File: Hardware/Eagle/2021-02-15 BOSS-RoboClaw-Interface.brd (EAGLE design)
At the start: 41.4 x 48.3 mm, 10 parts, among them IC1 ISO7221AQDRQ1, J1 MOLEX 22112024, J2 MOLEX 22122034, J3 Amphenol 75869-130LF, J5 SAMTEC ESQ-110-33-T-D, J6 SAMTEC-ESQ-105-33-T-S, X1 Amphenol L77SDAH15SOL2RM8C309

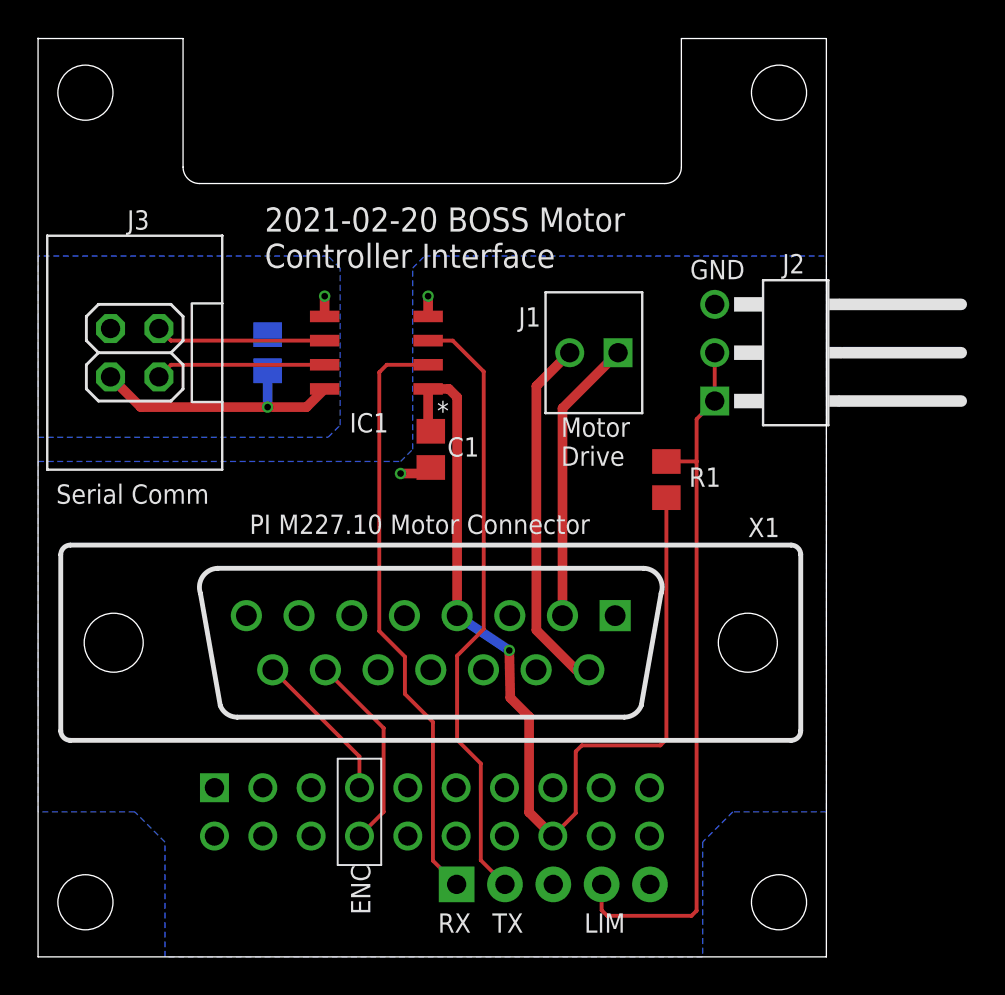
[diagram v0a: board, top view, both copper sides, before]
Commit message: Added pullup to limit switch line
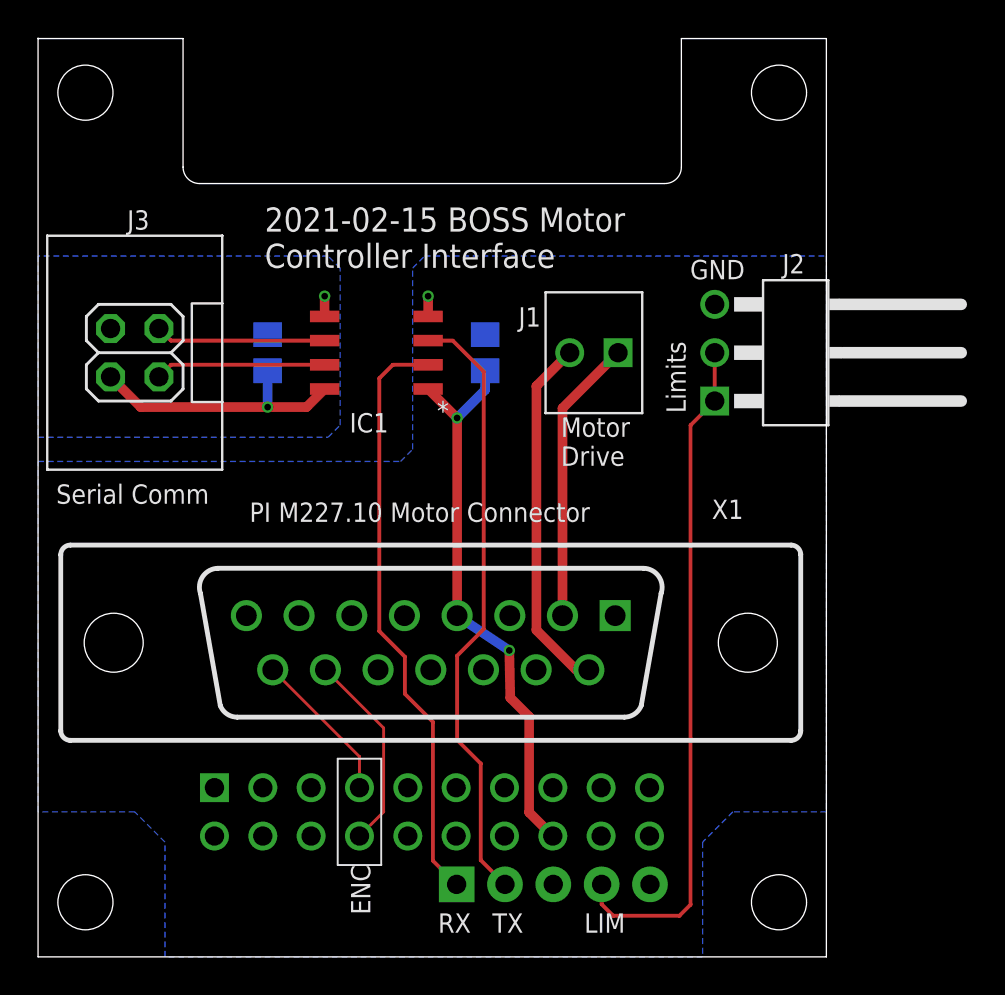
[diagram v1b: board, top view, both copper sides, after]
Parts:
- removed R1: 10K, AUmlib:R0805
- moved C1 5.83 mm to (23.5, 31.8), flipped to the bottom, turned to 90 degrees
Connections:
- removed net ROBO-RX: IC1.2, J6.1
- removed net ROBO0TX: IC1.3, J6.2
- new net RXMCU: IC1.6, J3.3
- new net TXMCU: IC1.7, J3.1
- net LIMIT: no longer R1.1
- net RX: now also IC1.2, J6.1; no longer IC1.7, J3.1
- net TX: now also IC1.3, J6.2; no longer IC1.6, J3.3
- net VCC1: no longer R1.2
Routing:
- net ROBO0TX: track 32.2 -> 0.00 mm
- net ROBO-RX: track 31.3 -> 0.00 mm
- net TX: track 8.98 -> 32.2 mm
- net VCC1: track 52.1 -> 29.6 mm, vias 1 -> 2
- net RX: track 8.98 -> 31.1 mm
- net RXMCU: track 0.00 -> 8.98 mm
- net TXMCU: track 0.00 -> 8.98 mm
- net LIMIT: track 37.9 -> 35.7 mm
- net GND: track 2.79 -> 1.07 mm, vias 2 -> 1
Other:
- board text added: "2021-02-15 BOSS Motor Controller Interface"
- board text added: "Limits"
- board text removed: "+5V"
- board text removed: "2021-02-20 BOSS Motor Controller Interface"
- board text removed: "GND -ISO"
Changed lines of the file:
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@@
 <wire x1="8.4836" y1="40.64" x2="32.9438" y2="40.64" width="0" layer="20"/>
 <wire x1="33.8074" y1="48.26" x2="41.4274" y2="48.26" width="0" layer="20"/>
-<text x="11.9126" y="36.2077" size="1.27" layer="21" font="vector">2021-02-20 BOSS Motor
+<text x="11.9126" y="36.2077" size="1.27" layer="21" font="vector">2021-02-15 BOSS Motor
 Controller Interface</text>
+<text x="34.036" y="28.575" size="1.016" layer="21" font="vector" rot="R90">Limits</text>
 <text x="34.2646" y="35.6108" size="1.016" layer="21" font="vector">GND</text>
 <text x="27.4828" y="25.8064" size="1.016" layer="21" font="vector">Motor
@@
 <wire x1="15.748" y1="4.826" x2="18.034" y2="4.826" width="0.1016" layer="21"/>
 <text x="0.9525" y="23.8125" size="1.016" layer="21" font="vector">Serial Comm</text>
-<text x="11.1125" y="22.225" size="1.016" layer="21" font="vector">PI M227.10 Motor Connector</text>
-<text x="9.2075" y="32.385" size="1.016" layer="22" rot="MR0">TX</text>
-<text x="9.2075" y="29.845" size="1.016" layer="22" rot="MR0">RX</text>
-<text x="4.7625" y="28.2575" size="1.016" layer="22" rot="MR0">+5V</text>
-<text x="5.08" y="34.29" size="1.016" layer="22" rot="MR0">GND
--ISO</text>
+<text x="11.1125" y="22.86" size="1.016" layer="21" font="vector">PI M227.10 Motor Connector</text>
 </plain>
 <attributes>
@@
 <attribute name="MF" value="" x="53.6575" y="10.16" size="1.778" layer="27" display="off"/>
 <attribute name="MPN" value="" x="53.6575" y="10.16" size="1.778" layer="27" display="off"/>
-<attribute name="NAME" x="37.3126" y="22.0599" size="1.016" layer="25"/>
+<attribute name="NAME" x="35.4076" y="23.0124" size="1.016" layer="25"/>
 <attribute name="OC_FARNELL" value="unknown" x="53.6575" y="10.16" size="1.778" layer="27" display="off"/>
 <attribute name="OC_NEWARK" value="unknown" x="53.6575" y="10.16" size="1.778" layer="27" display="off"/>
 </element>
-<element name="C1" library="AUmlib" library_urn="urn:adsk.eagle:library:9166017" package="C0805" package3d_urn="urn:adsk.eagle:package:4021265/3" value="0.1uF" x="20.6375" y="26.67" smashed="yes" rot="R270">
-<attribute name="NAME" x="23.1775" y="27.305" size="1.016" layer="25" font="vector" rot="R180"/>
-<attribute name="SPICEPREFIX" value="C" x="20.6375" y="26.67" size="1.778" layer="27" rot="R270" display="off"/>
+<element name="C1" library="AUmlib" library_urn="urn:adsk.eagle:library:9166017" package="C0805" package3d_urn="urn:adsk.eagle:package:4021265/3" value="0.1uF" x="23.495" y="31.75" smashed="yes" rot="MR90">
+<attribute name="NAME" x="24.13" y="33.9725" size="1.016" layer="26" font="vector" rot="MR0"/>
+<attribute name="SPICEPREFIX" value="C" x="23.495" y="31.75" size="1.778" layer="28" rot="MR90" display="off"/>
 </element>
 <element name="C2" library="AUmlib" library_urn="urn:adsk.eagle:library:9166017" package="C0805" package3d_urn="urn:adsk.eagle:package:4021265/3" value="0.1uF" x="12.065" y="31.75" smashed="yes" rot="MR90">
@@
 <element name="J5" library="AUmlib" library_urn="urn:adsk.eagle:library:9166017" package="2X10-ESQ-110-33-T-D" package3d_urn="urn:adsk.eagle:package:24929474/2" value="SAMTEC ESQ-110-33-T-D" x="20.701" y="7.62" smashed="yes" rot="MR180">
 <attribute name="NAME" x="5.7785" y="8.255" size="1.016" layer="26" rot="MR180"/>
-</element>
-<element name="R1" library="AUmlib" library_urn="urn:adsk.eagle:library:9166017" package="R0805" package3d_urn="urn:adsk.eagle:package:4021199/4" value="10K" x="33.02" y="25.0825" smashed="yes" rot="R270">
-<attribute name="NAME" x="35.8775" y="25.7175" size="1.016" layer="25" font="vector" rot="R180"/>
-<attribute name="SPICEPREFIX" value="R" x="33.02" y="25.0825" size="1.778" layer="27" rot="R270" display="off"/>
 </element>
 </elements>
@@
 <contactref element="X1" pad="6"/>
 <contactref element="J5" pad="15"/>
-<wire x1="20.6375" y1="25.72" x2="20.3175" y2="25.4" width="0.508" layer="1"/>
-<wire x1="20.3175" y1="25.4" x2="19.05" y2="25.4" width="0.508" layer="1"/>
-<via x="19.05" y="25.4" extent="1-16" drill="0.35"/>
-</signal>
-<signal name="ROBO-RX">
+</signal>
+<signal name="RX">
 <contactref element="IC1" pad="2"/>
 <wire x1="20.7518" y1="12.3444" x2="19.2786" y2="13.8176" width="0.2032" layer="1"/>
-<wire x1="18.3261" y1="31.115" x2="20.4978" y2="31.115" width="0.2032" layer="1"/>
+<wire x1="18.6436" y1="31.115" x2="20.4978" y2="31.115" width="0.2032" layer="1"/>
 <wire x1="20.7518" y1="5.0546" x2="20.7518" y2="12.3444" width="0.2032" layer="1"/>
 <wire x1="19.2786" y1="13.8176" x2="19.2786" y2="15.7734" width="0.2032" layer="1"/>
 <wire x1="19.2786" y1="15.7734" x2="17.9324" y2="17.1196" width="0.2032" layer="1"/>
-<wire x1="17.9324" y1="17.1196" x2="17.9324" y2="30.7213" width="0.2032" layer="1"/>
-<wire x1="17.9324" y1="30.7213" x2="18.3261" y2="31.115" width="0.2032" layer="1"/>
+<wire x1="17.9324" y1="17.1196" x2="17.9324" y2="30.4038" width="0.2032" layer="1"/>
+<wire x1="17.9324" y1="30.4038" x2="18.6436" y2="31.115" width="0.2032" layer="1"/>
 <contactref element="J6" pad="1"/>
 <wire x1="21.9964" y1="3.81" x2="20.7518" y2="5.0546" width="0.2032" layer="1"/>
 </signal>
-<signal name="ROBO0TX">
+<signal name="TX">
 <contactref element="IC1" pad="3"/>
 <wire x1="20.4978" y1="32.385" x2="21.7932" y2="32.385" width="0.2032" layer="1"/>
@@
 <contactref element="J2" pad="2"/>
 <wire x1="35.56" y1="31.75" x2="35.56" y2="29.21" width="0.2032" layer="1"/>
-<wire x1="35.56" y1="29.21" x2="34.6075" y2="28.257496875" width="0.2032" layer="1"/>
-<wire x1="34.6075" y1="2.4257" x2="34.3408" y2="2.159" width="0.2032" layer="1"/>
-<wire x1="34.6075" y1="28.257496875" x2="34.6075" y2="26.035" width="0.2032" layer="1"/>
-<wire x1="34.6075" y1="26.035" x2="34.6075" y2="2.4257" width="0.2032" layer="1"/>
-<wire x1="34.3408" y1="2.159" x2="29.9085" y2="2.159" width="0.2032" layer="1"/>
-<wire x1="29.6164" y1="2.4511" x2="29.9085" y2="2.159" width="0.2032" layer="1"/>
+<wire x1="35.56" y1="29.21" x2="34.29" y2="27.93999375" width="0.2032" layer="1"/>
+<wire x1="34.29" y1="2.7432" x2="33.7058" y2="2.159" width="0.2032" layer="1"/>
+<wire x1="34.29" y1="27.93999375" x2="34.29" y2="2.7432" width="0.2032" layer="1"/>
+<wire x1="33.7058" y1="2.159" x2="30.226" y2="2.159" width="0.2032" layer="1"/>
+<wire x1="29.6164" y1="2.7686" x2="30.226" y2="2.159" width="0.2032" layer="1"/>
 <contactref element="J6" pad="4"/>
-<wire x1="29.6164" y1="3.81" x2="29.6164" y2="2.4511" width="0.2032" layer="1"/>
-<contactref element="R1" pad="1"/>
-<wire x1="33.02" y1="26.0325" x2="33.0225" y2="26.035" width="0.2032" layer="1"/>
-<wire x1="33.0225" y1="26.035" x2="34.6075" y2="26.035" width="0.2032" layer="1"/>
+<wire x1="29.6164" y1="3.81" x2="29.6164" y2="2.7686" width="0.2032" layer="1"/>
 </signal>
 <signal name="VCC2">
@@
 <via x="24.765" y="16.1036" extent="1-16" drill="0.35"/>
 <wire x1="24.765" y1="16.1036" x2="22.0218" y2="17.9324" width="0.508" layer="16"/>
+<wire x1="22.0218" y1="17.9324" x2="22.0218" y2="28.321" width="0.508" layer="1"/>
+<via x="22.0218" y="28.321" extent="1-16" drill="0.35"/>
+<wire x1="23.495" y1="30.8" x2="23.495" y2="29.7942" width="0.508" layer="16"/>
+<wire x1="23.495" y1="29.7942" x2="22.0218" y2="28.321" width="0.508" layer="16"/>
 <contactref element="J5" pad="16"/>
 <wire x1="25.8064" y1="7.5946" x2="27.051" y2="6.35" width="0.508" layer="1"/>
 <wire x1="25.8064" y1="12.6238" x2="25.8064" y2="7.5946" width="0.508" layer="1"/>
 <contactref element="IC1" pad="1"/>
-<contactref element="R1" pad="2"/>
-<wire x1="22.0218" y1="17.9324" x2="22.0218" y2="29.4132" width="0.508" layer="1"/>
-<wire x1="21.59" y1="29.845" x2="20.4978" y2="29.845" width="0.508" layer="1"/>
-<wire x1="22.0218" y1="29.4132" x2="21.59" y2="29.845" width="0.508" layer="1"/>
-<wire x1="20.4978" y1="29.845" x2="20.4978" y2="27.7597" width="0.508" layer="1"/>
-<wire x1="20.4978" y1="27.7597" x2="20.6375" y2="27.62" width="0.508" layer="1"/>
-<wire x1="27.051" y1="6.35" x2="28.2575" y2="7.5565" width="0.2032" layer="1"/>
-<wire x1="28.2575" y1="10.795" x2="28.575" y2="11.1125" width="0.2032" layer="1"/>
-<wire x1="28.575" y1="11.1125" x2="32.7025" y2="11.1125" width="0.2032" layer="1"/>
-<wire x1="32.7025" y1="11.1125" x2="33.02" y2="11.43" width="0.2032" layer="1"/>
-<wire x1="33.02" y1="11.43" x2="33.02" y2="24.1325" width="0.2032" layer="1"/>
-<wire x1="28.2575" y1="7.5565" x2="28.2575" y2="10.795" width="0.2032" layer="1"/>
+<wire x1="20.4978" y1="29.845" x2="22.0218" y2="28.321" width="0.508" layer="1"/>
 </signal>
 <signal name="GND-ISO">
@@
 <via x="15.0622" y="34.7218" extent="1-16" drill="0.35"/>
 </signal>
-<signal name="RX">
+<signal name="TXMCU">
 <contactref element="IC1" pad="7"/>
 <contactref element="J3" pad="1"/>
@@
 <wire x1="15.0622" y1="31.115" x2="6.985" y2="31.115" width="0.2032" layer="1"/>
 </signal>
-<signal name="TX">
+<signal name="RXMCU">
 <contactref element="IC1" pad="6"/>
 <contactref element="J3" pad="3"/>
@@
 <contactref element="J5" pad="8"/>
 <contactref element="X1" pad="14"/>
-<wire x1="15.1003" y1="15.0876" x2="18.161" y2="12.0269" width="0.2032" layer="1"/>
-<wire x1="18.161" y1="7.62" x2="16.891" y2="6.35" width="0.2032" layer="1"/>
-<wire x1="18.161" y1="12.0269" x2="18.161" y2="7.62" width="0.2032" layer="1"/>
+<wire x1="15.1003" y1="15.0876" x2="18.161" y2="12.0269" width="0.1524" layer="1"/>
+<wire x1="18.161" y1="7.62" x2="16.891" y2="6.35" width="0.1524" layer="1"/>
+<wire x1="18.161" y1="12.0269" x2="18.161" y2="7.62" width="0.1524" layer="1"/>
 </signal>
 <signal name="ENC1B">
 <contactref element="J5" pad="7"/>
 <contactref element="X1" pad="15"/>
-<wire x1="12.3317" y1="15.0876" x2="16.891" y2="10.5283" width="0.2032" layer="1"/>
-<wire x1="16.891" y1="10.5283" x2="16.891" y2="8.89" width="0.2032" layer="1"/>
+<wire x1="12.3317" y1="15.0876" x2="16.891" y2="10.5283" width="0.1524" layer="1"/>
+<wire x1="16.891" y1="10.5283" x2="16.891" y2="8.89" width="0.1524" layer="1"/>
 </signal>
 </signals>
